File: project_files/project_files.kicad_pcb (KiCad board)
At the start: 2 copper layers, 27 parts, among them SW11 SW_Push, SW12 SW_Push, SW13 SW_Push, SW17 SW_Push, SW18 SW_Push, SW19 SW_Push, SW3 SW_Push, SW4 SW_Push, SW5 SW_Push, SW7 SW_Push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

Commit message: more pcb work
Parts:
- moved U1 4.95 mm to (209.1, 50.3)
- moved SongSelect1 3.89 mm to (87.8, 64.1)
- moved OLED1 1.84 mm to (133.5, 60.8)
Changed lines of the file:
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@@
 	(footprint "KiCad-SSD1306-0.91-OLED-4pin-128x32:SSD1306-0.91-OLED-4pin-128x32"
 		(layer "F.Cu")
-		(at 134.95 61.945)
+		(at 133.515 60.79)
 		(property "Reference" "OLED1"
 			(at 1.9 5.91 90)
@@
 	(footprint "Rotary_Encoder:RotaryEncoder_Alps_EC11E-Switch_Vertical_H20mm"
 		(layer "F.Cu")
-		(at 87.75 60.25)
+		(at 87.75 64.14191)
 		(descr "Alps rotary encoder, EC12E... with switch, vertical shaft, http://www.alps.com/prod/info/E/HTML/Encoder/Incremental/EC11/EC11E15204A3.html")
 		(tags "rotary encoder")
@@
 	(footprint "footprints:XIAO-Generic-Hybrid-14P-2.54-21X17.8MM"
 		(layer "B.Cu")
-		(at 214 50 180)
+		(at 209.052815 50.267925 180)
 		(property "Reference" "U1"
 			(at 0 -2.54 0)

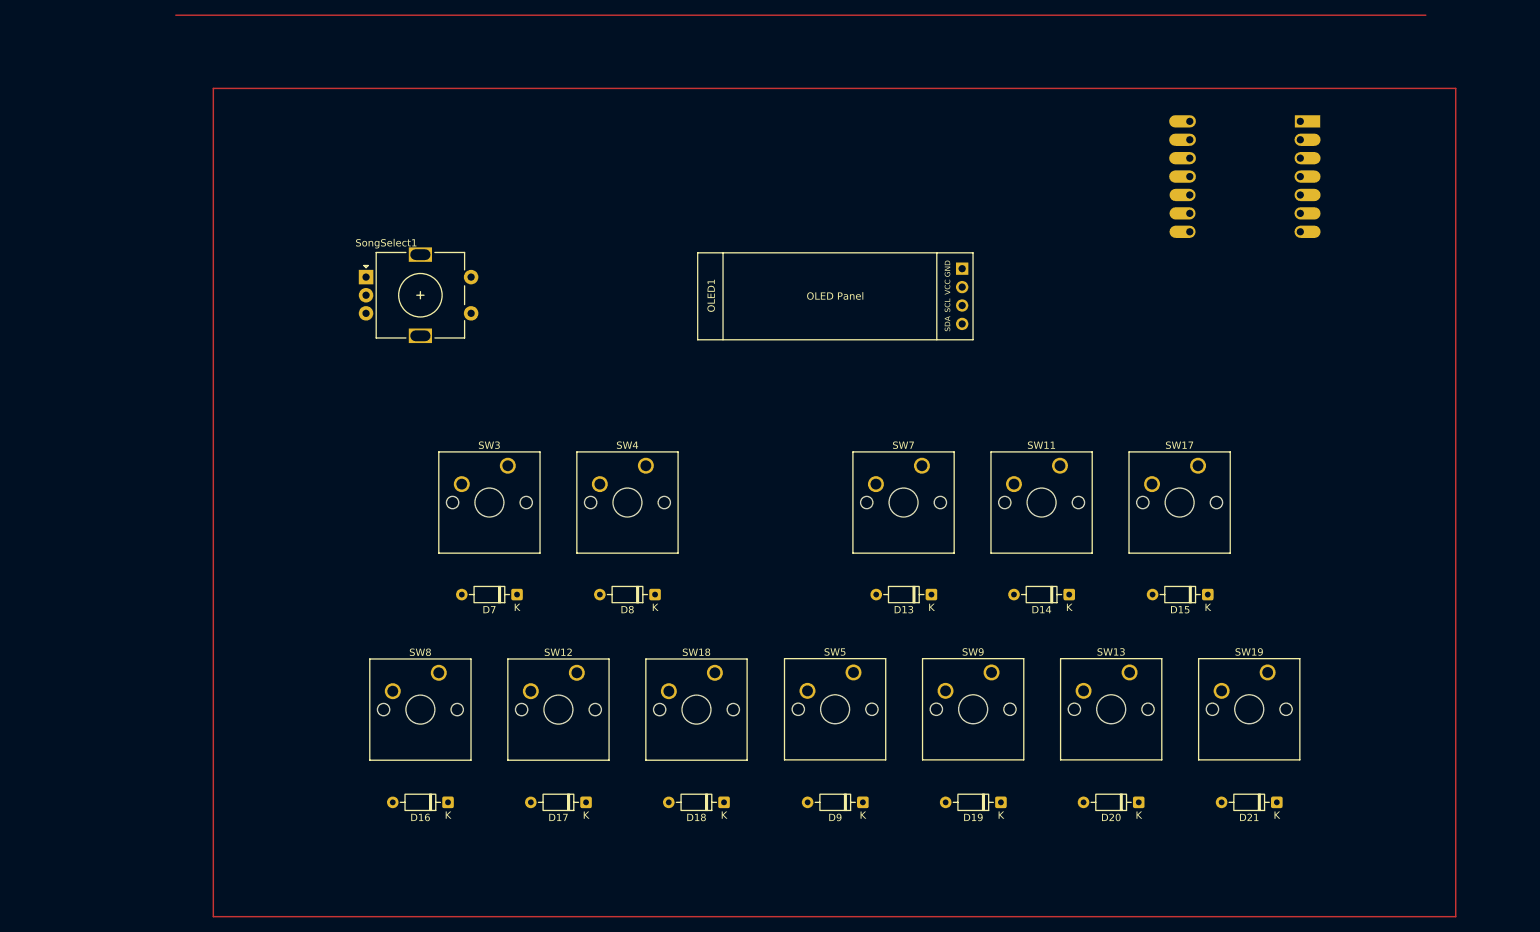
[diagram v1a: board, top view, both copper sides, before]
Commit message: pcb done
pcb too big
might have to scrap the project entirely
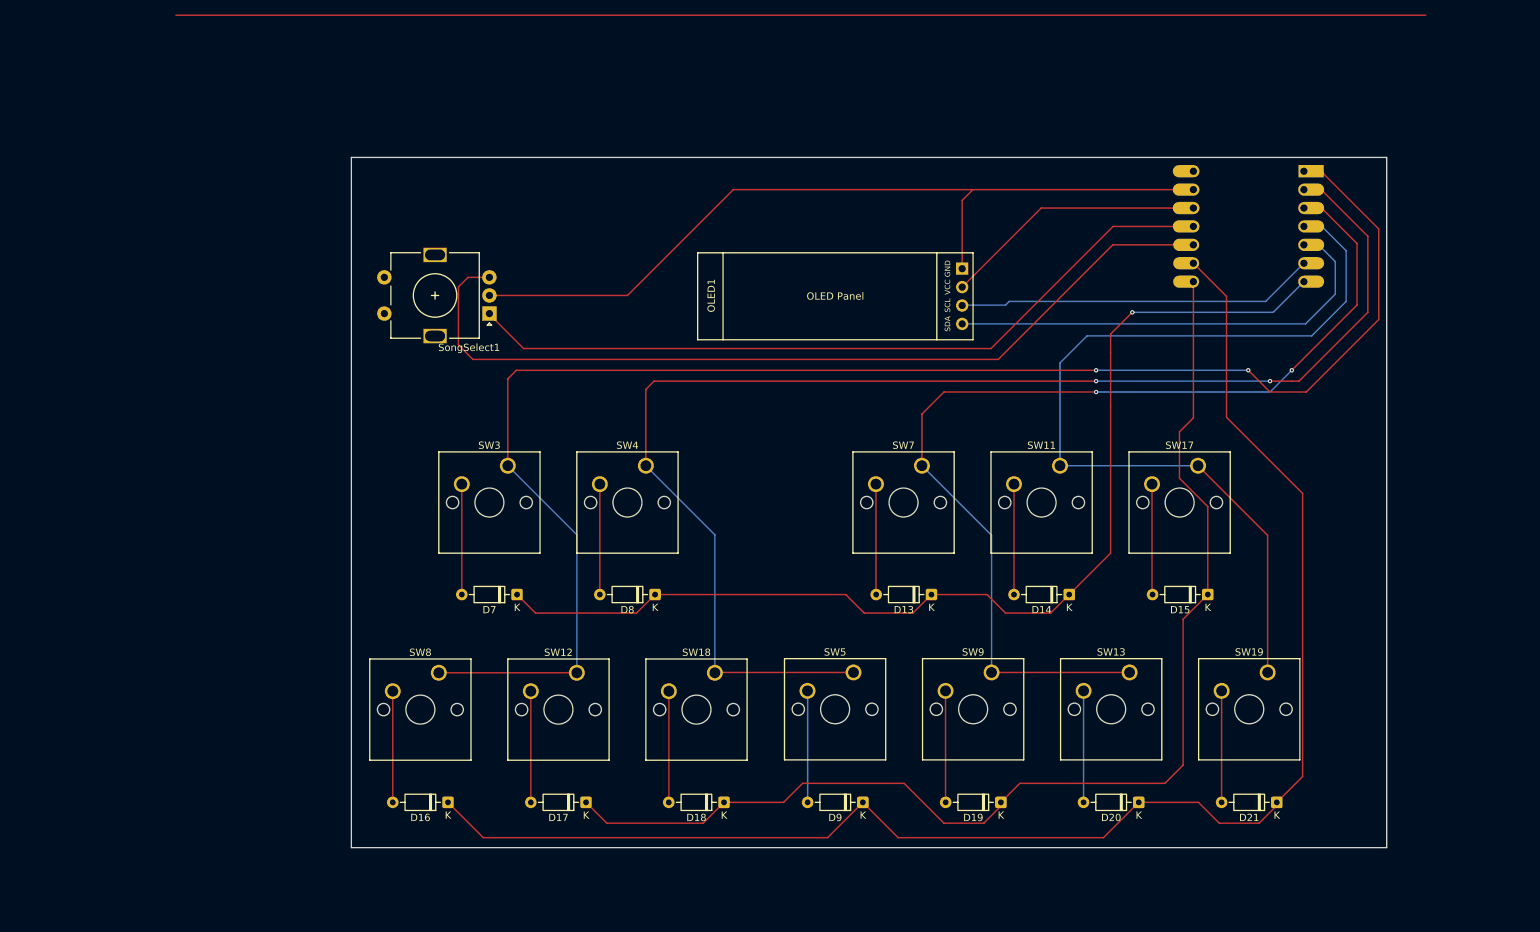
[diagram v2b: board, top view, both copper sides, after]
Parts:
- moved SongSelect1 17.8 mm to (104.8, 69.2), turned to 180 degrees
- moved U1 6.90 mm to (209.6, 57.1)
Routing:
- net /PIN_1: track 0.00 -> 215.7 mm, vias 0 -> 2
- net /PIN_9: track 0.00 -> 207.2 mm
- net /PIN_2: track 0.00 -> 188.2 mm, vias 0 -> 2
- net /PIN_8: track 0.00 -> 162.3 mm
- net /PIN_7: track 0.00 -> 150.5 mm, vias 0 -> 1
- net /PIN_3: track 0.00 -> 142.8 mm, vias 0 -> 2
- net /PIN_4: track 0.00 -> 123.0 mm
- net /PIN_10: track 0.00 -> 121.6 mm
- net GND: track 0.00 -> 114.7 mm
- net /PIN_11: track 0.00 -> 106.2 mm
- net /SDA: track 0.00 -> 63.0 mm
- net /SCL: track 0.00 -> 49.6 mm
- net /PWR_3v3: track 0.00 -> 36.4 mm
- net Net-(D9-A): track 0.00 -> 15.4 mm
- net Net-(D20-A): track 0.00 -> 15.4 mm
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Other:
- board outline added: 142.9 x 95.2 mm

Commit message: new pcb design
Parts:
- moved SongSelect1 108.9 mm to (212.0, 50.1)
- moved OLED1 93.7 mm to (224.4, 83.5), turned to 90 degrees
- moved D16 68.2 mm to (52.6, 86.7)
- moved D17 68.2 mm to (71.6, 86.7)
- moved D18 68.2 mm to (90.7, 86.7)
- moved D19 68.2 mm to (128.9, 86.7)
- moved D9 68.2 mm to (109.8, 86.7)
- moved D13 68.1 mm to (119.3, 58.2)
- moved D8 68.1 mm to (81.2, 58.2)
- moved D7 68.1 mm to (62.1, 58.2)
- moved SW12 65.8 mm to (70.4, 72.1)
- moved SW7 65.8 mm to (118.0, 43.5)
- moved SW8 65.8 mm to (51.3, 72.1)
- moved SW9 65.8 mm to (127.6, 72.1)
- moved SW3 65.8 mm to (60.9, 43.5)
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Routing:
- net /PIN_10: track 121.6 -> 21.3 mm
- net GND: track 114.7 -> 16.9 mm
- net /PIN_11: track 106.2 -> 11.2 mm
- net /SDA: track 63.0 -> 6.72 mm
- net /PIN_9: track 207.2 -> 163.2 mm, vias 0 -> 2
- net /SCL: track 49.6 -> 10.3 mm
- net /PWR_3v3: track 36.4 -> 7.19 mm
- net /PIN_1: track 215.7 -> 242.5 mm
- net /PIN_8: track 162.3 -> 145.0 mm, vias 0 -> 2
- net /PIN_2: track 188.2 -> 192.4 mm
- net /PIN_7: track 150.5 -> 154.1 mm, vias 1 -> 2
- net Net-(D21-A): track 15.4 -> 12.1 mm
- net Net-(D17-A): track 15.3 -> 12.1 mm
- net Net-(D16-A): track 15.3 -> 12.1 mm
- net Net-(D19-A): track 15.4 -> 12.1 mm
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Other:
- board size 142.9 x 95.2 mm -> 208.5 x 53.4 mm

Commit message: pcb done maybe
kudos anicetus
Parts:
- added ?: , , F.Cu at (99.0, 68.6)
- added ?: , , F.Cu at (108.6, 93.6)
- added ?: , , F.Cu at (108.6, 96.0)
- added ?: , , F.Cu at (194.3, 131.3)
- added ?: , , F.Cu at (184.8, 124.6)
- added ?: , , F.Cu at (194.3, 148.4)
- added ?: , , F.Cu at (99.0, 65.0)
- added ?: , , F.Cu at (184.8, 117.4)
- added ?: , , F.Cu at (194.3, 146.0)
- added ?: , , F.Cu at (184.8, 121.0)
- added ?: , , F.Cu at (108.6, 78.9)
- added ?: , , F.Cu at (99.0, 72.2)
- added REF**: BreakLine_11h_D0.5mm_P0.85mm, Panelization:BreakLine_11h_D0.5mm_P0.85mm, F.Cu at (179.0, 98.4)
- added REF**: BreakLine_11h_D0.5mm_P0.85mm, Panelization:BreakLine_11h_D0.5mm_P0.85mm, F.Cu at (132.2, 98.4)
- added REF**: BreakLine_11h_D0.5mm_P0.85mm, Panelization:BreakLine_11h_D0.5mm_P0.85mm, F.Cu at (113.5, 98.4)
- added REF**: BreakLine_11h_D0.5mm_P0.85mm, Panelization:BreakLine_11h_D0.5mm_P0.85mm, F.Cu at (141.6, 98.4)
- added REF**: BreakLine_11h_D0.5mm_P0.85mm, Panelization:BreakLine_11h_D0.5mm_P0.85mm, F.Cu at (122.9, 98.4)
- added REF**: BreakLine_1h_D0.5mm_P0.85mm, Panelization:BreakLine_1h_D0.5mm_P0.85mm, F.Cu at (184.1, 98.4)
- added REF**: BreakLine_11h_D0.5mm_P0.85mm, Panelization:BreakLine_11h_D0.5mm_P0.85mm, F.Cu at (169.6, 98.4)
- added REF**: BreakLine_11h_D0.5mm_P0.85mm, Panelization:BreakLine_11h_D0.5mm_P0.85mm, F.Cu at (160.3, 98.4)
- added REF**: BreakLine_11h_D0.5mm_P0.85mm, Panelization:BreakLine_11h_D0.5mm_P0.85mm, F.Cu at (150.9, 98.4)
- Rotary Encoder: renamed from SongSelect1
- moved D16 84.2 mm to (112.4, 146.0)
- moved D17 84.2 mm to (131.4, 146.0)
- moved D8 84.2 mm to (141.0, 117.4)
- moved SW5 84.2 mm to (168.3, 131.3)
- moved D7 84.2 mm to (121.9, 117.4)
- moved SW18 84.2 mm to (149.2, 131.4)
- moved SW3 84.2 mm to (120.6, 102.8)
- moved SW8 84.2 mm to (111.1, 131.4)
- moved D13 84.2 mm to (179.1, 117.4)
- moved D18 84.2 mm to (150.5, 146.0)
- moved D19 84.2 mm to (188.7, 146.0)
- moved D9 84.2 mm to (169.6, 146.0)
- moved SW12 84.2 mm to (130.2, 131.4)
- moved SW4 84.2 mm to (139.7, 102.8)
- moved SW7 84.2 mm to (177.8, 102.8)
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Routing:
- net GND: track 16.9 -> 78.4 mm
- net /PWR_3v3: track 7.19 -> 67.4 mm
- net /SDA: track 6.72 -> 34.4 mm
- net /SCL: track 10.3 -> 30.8 mm
- net /PIN_1: track 242.5 -> 238.3 mm, vias 2 -> 0
- net /PIN_8: track 145.0 -> 143.0 mm, vias 2 -> 0
- net /PIN_2: track 192.4 -> 190.7 mm, vias 2 -> 0
- net /PIN_9: track 163.2 -> 161.5 mm, vias 2 -> 0
- net /PIN_3: track 142.3 -> 140.9 mm, vias 2 -> 0
- net /PIN_7: track 154.1 -> 152.7 mm, vias 2 -> 0
- net /PIN_4: track 120.3 -> 119.3 mm
- net /PIN_11: track 11.2 -> 10.2 mm
- net /PIN_10: track 21.3 -> 20.4 mm
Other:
- board size 208.5 x 53.4 mm -> 95.3 x 104.8 mm

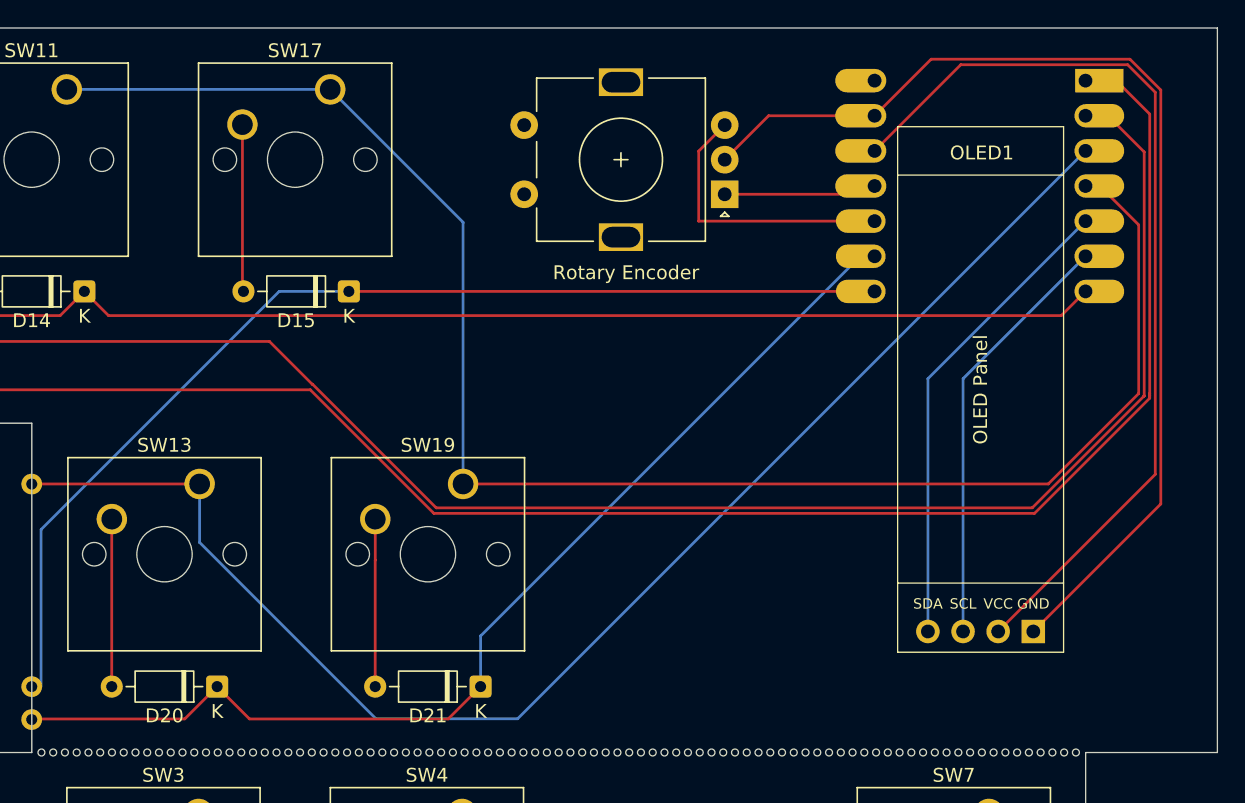
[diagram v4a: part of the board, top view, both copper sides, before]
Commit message: gerbers
castellated holes are really expensive though so there's gonna have to be a slight redesign
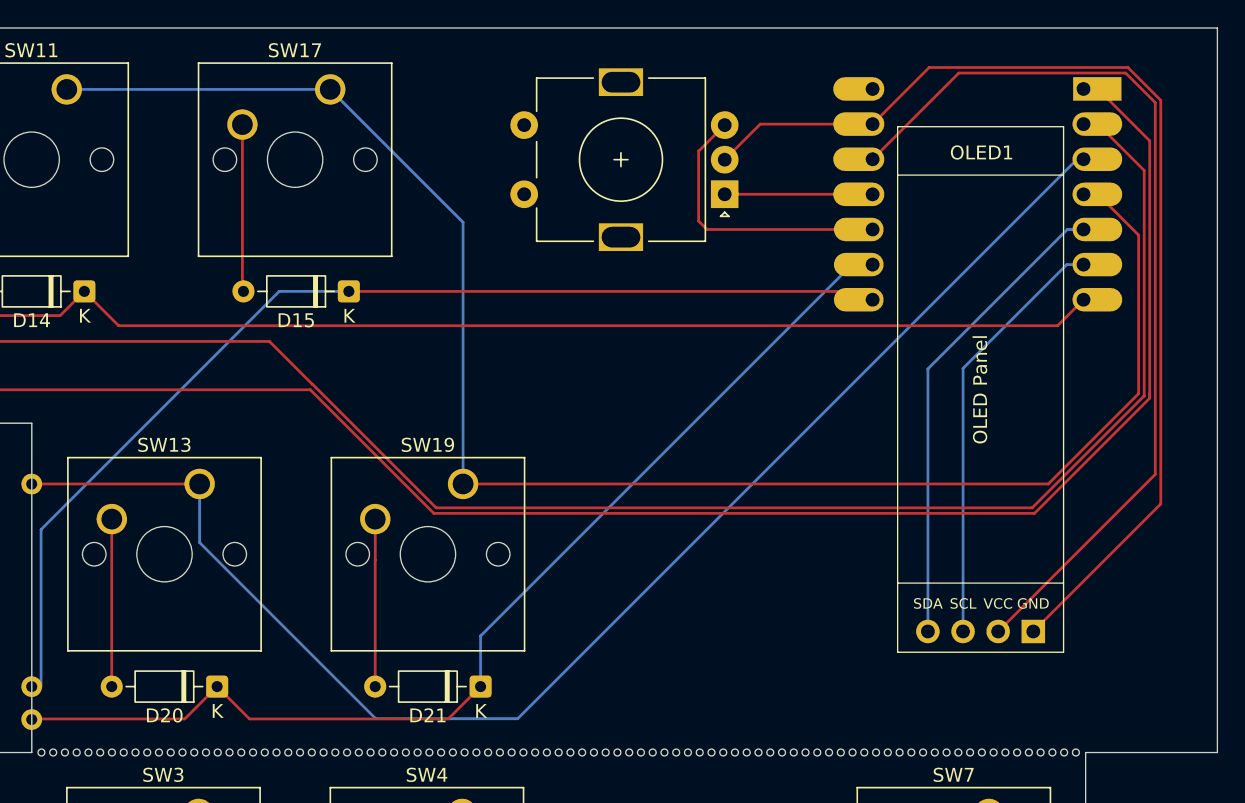
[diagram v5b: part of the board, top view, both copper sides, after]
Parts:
- SongSelect1: renamed from Rotary Encoder
- moved U1 0.62 mm to (177.0, 58.0)
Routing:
- net GND: track 78.4 -> 77.5 mm
- net /PIN_9: track 161.5 -> 160.6 mm
- net /PIN_3: track 140.9 -> 140.0 mm
- net /PIN_8: track 143.0 -> 142.3 mm
- net /PIN_4: track 119.3 -> 118.7 mm
- net /PWR_3v3: track 67.4 -> 66.8 mm

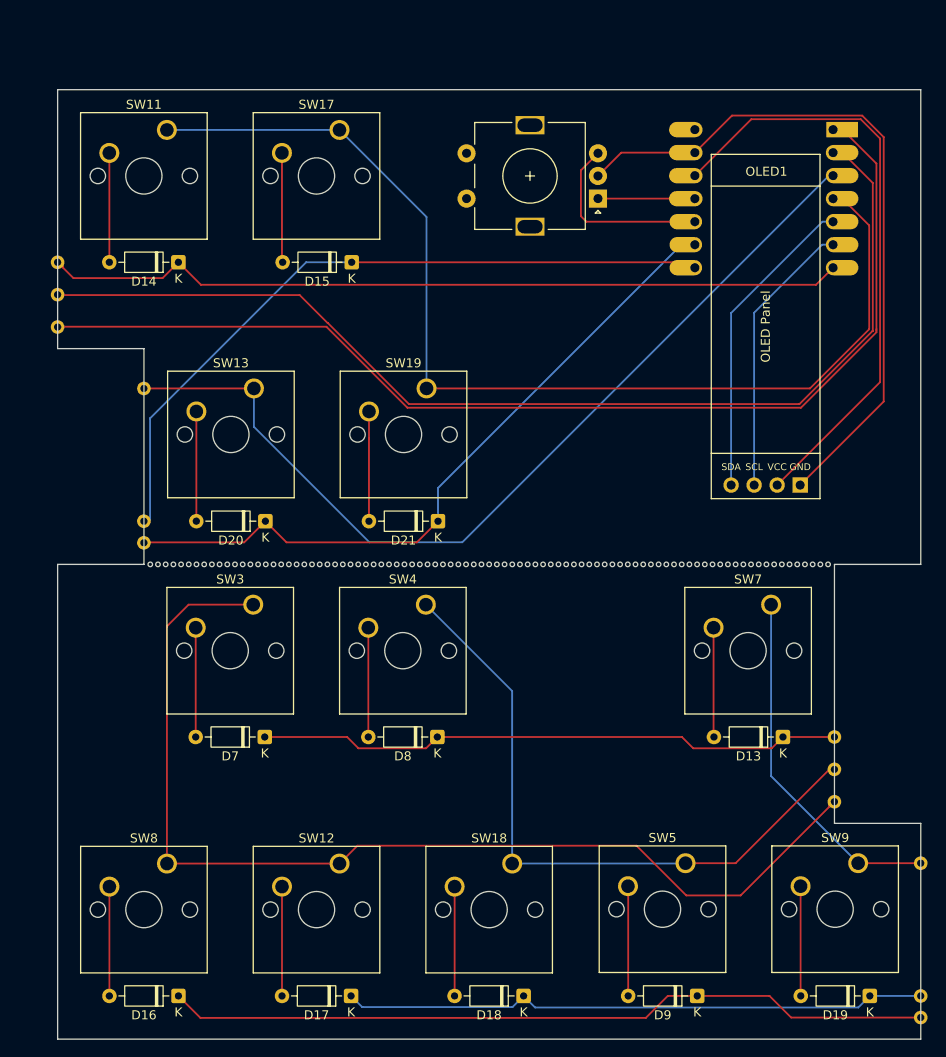
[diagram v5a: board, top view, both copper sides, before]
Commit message: test pads
no more castellated holes
my wallet is saved
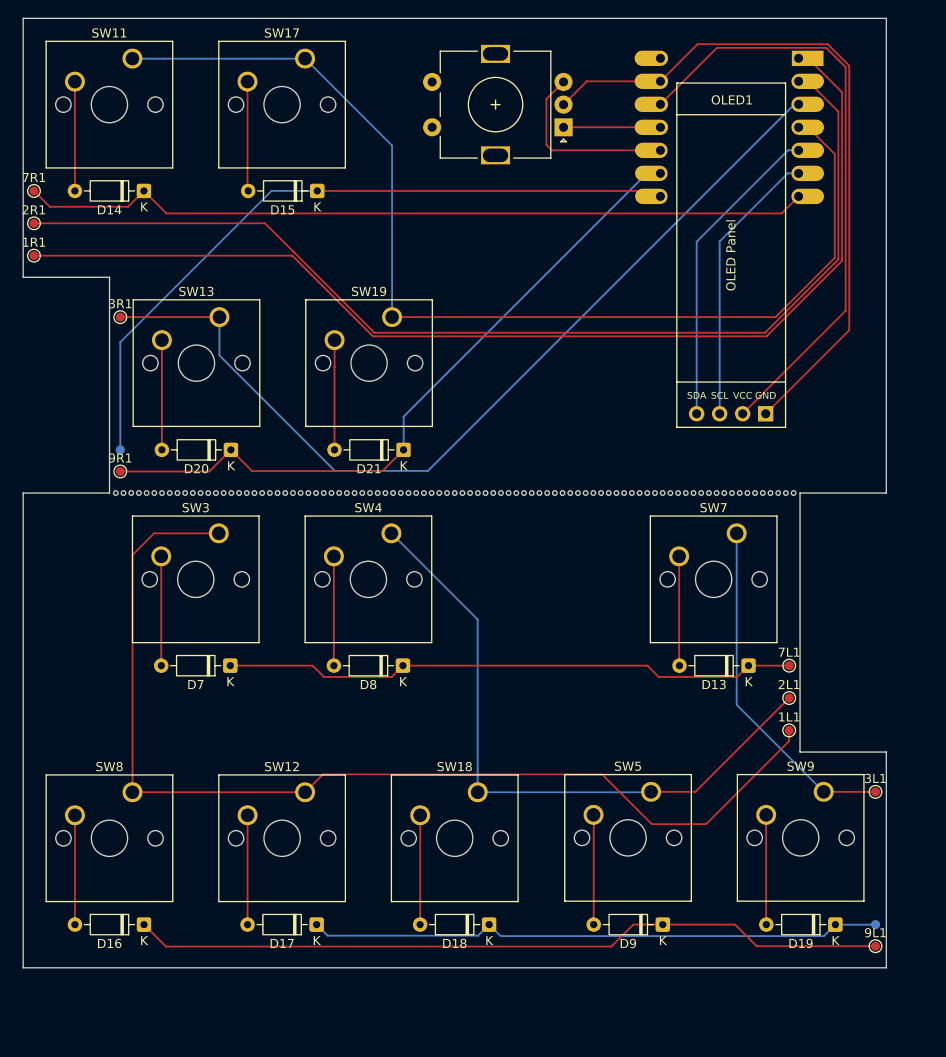
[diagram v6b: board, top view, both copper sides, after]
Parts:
- removed ? (x12): , 
- added 1L1: TestPoint, TestPoint:TestPoint_Pad_D1.0mm, F.Cu at (179.8, 116.7)
- added 1R1: TestPoint, TestPoint:TestPoint_Pad_D1.0mm, F.Cu at (96.4, 64.3)
- added 2L1: TestPoint, TestPoint:TestPoint_Pad_D1.0mm, F.Cu at (179.8, 113.1)
- added 2R1: TestPoint, TestPoint:TestPoint_Pad_D1.0mm, F.Cu at (96.4, 60.7)
- added 3L1: TestPoint, TestPoint:TestPoint_Pad_D1.0mm, F.Cu at (189.3, 123.5)
- added 3R1: TestPoint, TestPoint:TestPoint_Pad_D1.0mm, F.Cu at (106.0, 71.1)
- added 7L1: TestPoint, TestPoint:TestPoint_Pad_D1.0mm, F.Cu at (179.8, 109.5)
- added 7R1: TestPoint, TestPoint:TestPoint_Pad_D1.0mm, F.Cu at (96.4, 57.1)
- added 8L1: TestPoint, TestPoint:TestPoint_Pad_D1.0mm, B.Cu at (189.3, 138.1)
- added 8R1: TestPoint, TestPoint:TestPoint_Pad_D1.0mm, B.Cu at (106.0, 85.7)
- added 9L1: TestPoint, TestPoint:TestPoint_Pad_D1.0mm, F.Cu at (189.3, 140.5)
- added 9R1: TestPoint, TestPoint:TestPoint_Pad_D1.0mm, F.Cu at (106.0, 88.1)
- moved D16 8.74 mm to (108.6, 138.1)
- moved D19 8.74 mm to (184.9, 138.1)
- moved D8 8.74 mm to (137.2, 109.5)
- moved D17 8.74 mm to (127.6, 138.1)
- moved D7 8.74 mm to (118.1, 109.5)
- moved D14 8.74 mm to (108.6, 57.1)
- moved D13 8.74 mm to (175.3, 109.5)
- moved D15 8.74 mm to (127.7, 57.1)
- moved D18 8.74 mm to (146.7, 138.1)
- moved D21 8.74 mm to (137.2, 85.7)
- moved D9 8.74 mm to (165.8, 138.1)
- moved REF** 8.74 mm to (109.7, 90.5)
- moved REF** 8.74 mm to (165.8, 90.5)
- moved REF** 8.74 mm to (156.5, 90.5)
- moved REF** 8.74 mm to (147.1, 90.5)
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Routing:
- net /PIN_7: track 152.9 -> 151.4 mm
- net /PIN_3: track 140.0 -> 138.9 mm
- net /PIN_9: track 160.6 -> 159.5 mm
- net /PIN_2: track 190.4 -> 189.3 mm
- net /PIN_1: track 238.2 -> 237.5 mm
- net /PIN_8: track 142.3 -> 141.5 mm
